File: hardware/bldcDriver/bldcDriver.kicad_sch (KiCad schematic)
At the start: 101 parts, among them J1 Conn_01x02, J2 Conn_01x06, J3 Conn_01x06, J4 Conn_01x03, J5 Conn_01x06, Q13 PMOS, Q14 S8050, U10 AMS1117, U2 STM32G431RBTx, U3 TPS5430DDA, U5 MPU6500, U6 TLV9062xD, U7 MT3608, U8 TLV9062xD, U9 TLV9062xD, Y1 25MHz

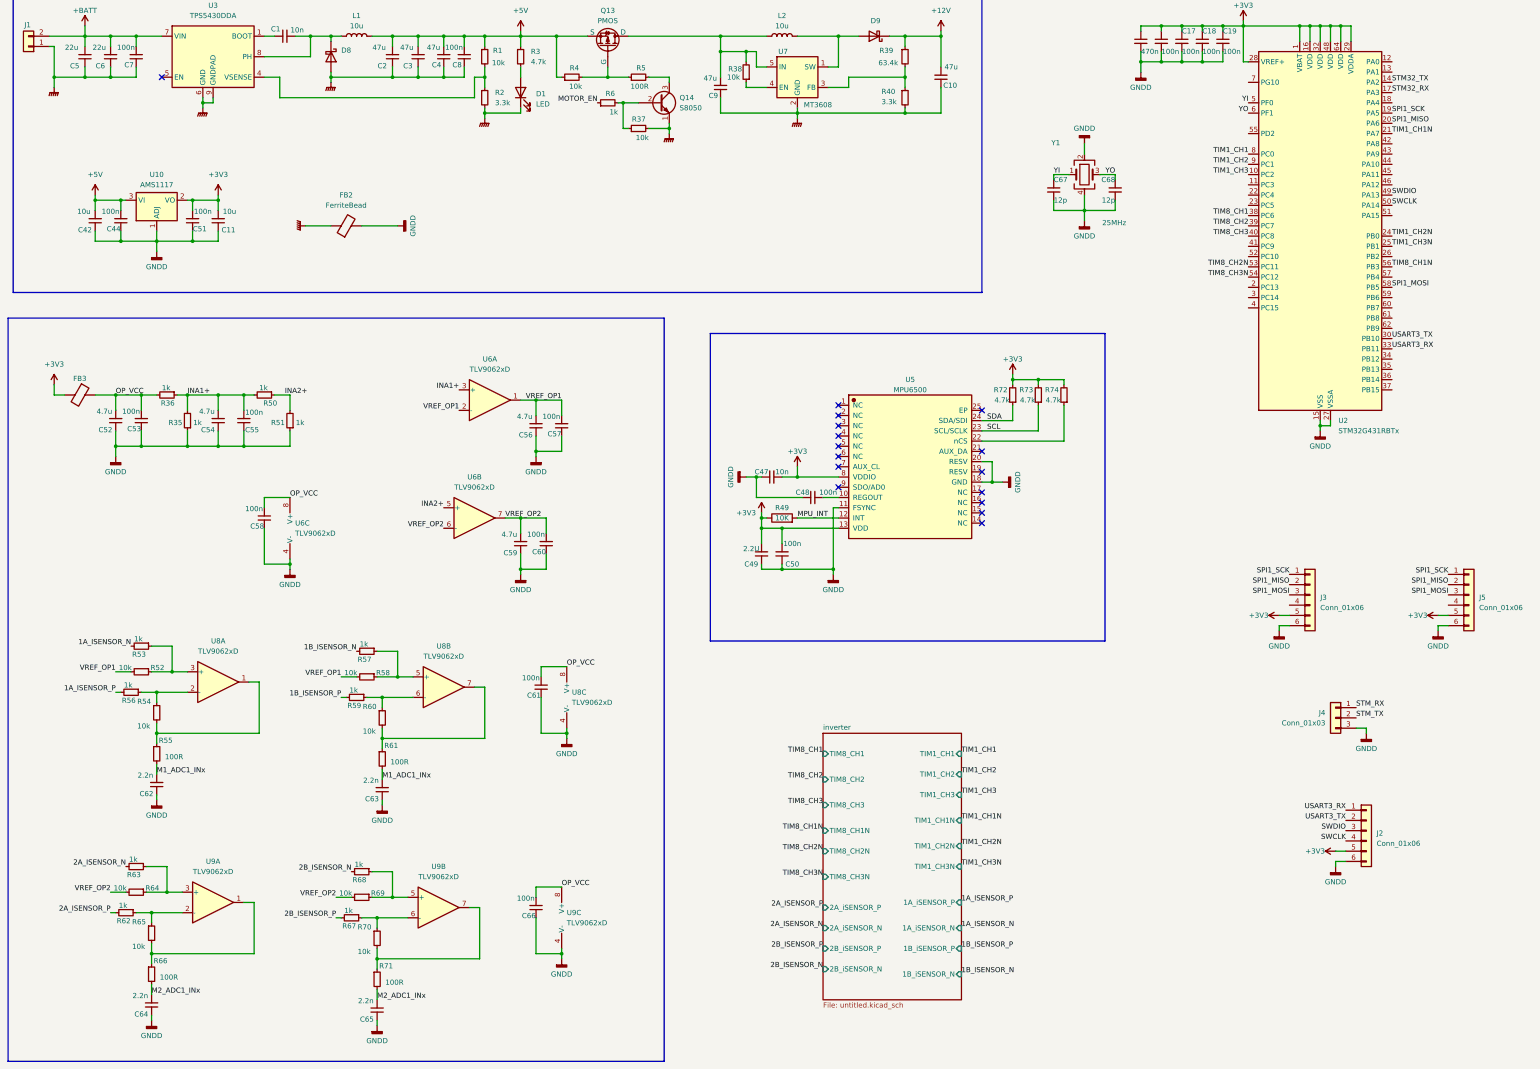
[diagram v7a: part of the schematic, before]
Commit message: update motorDriver pcb
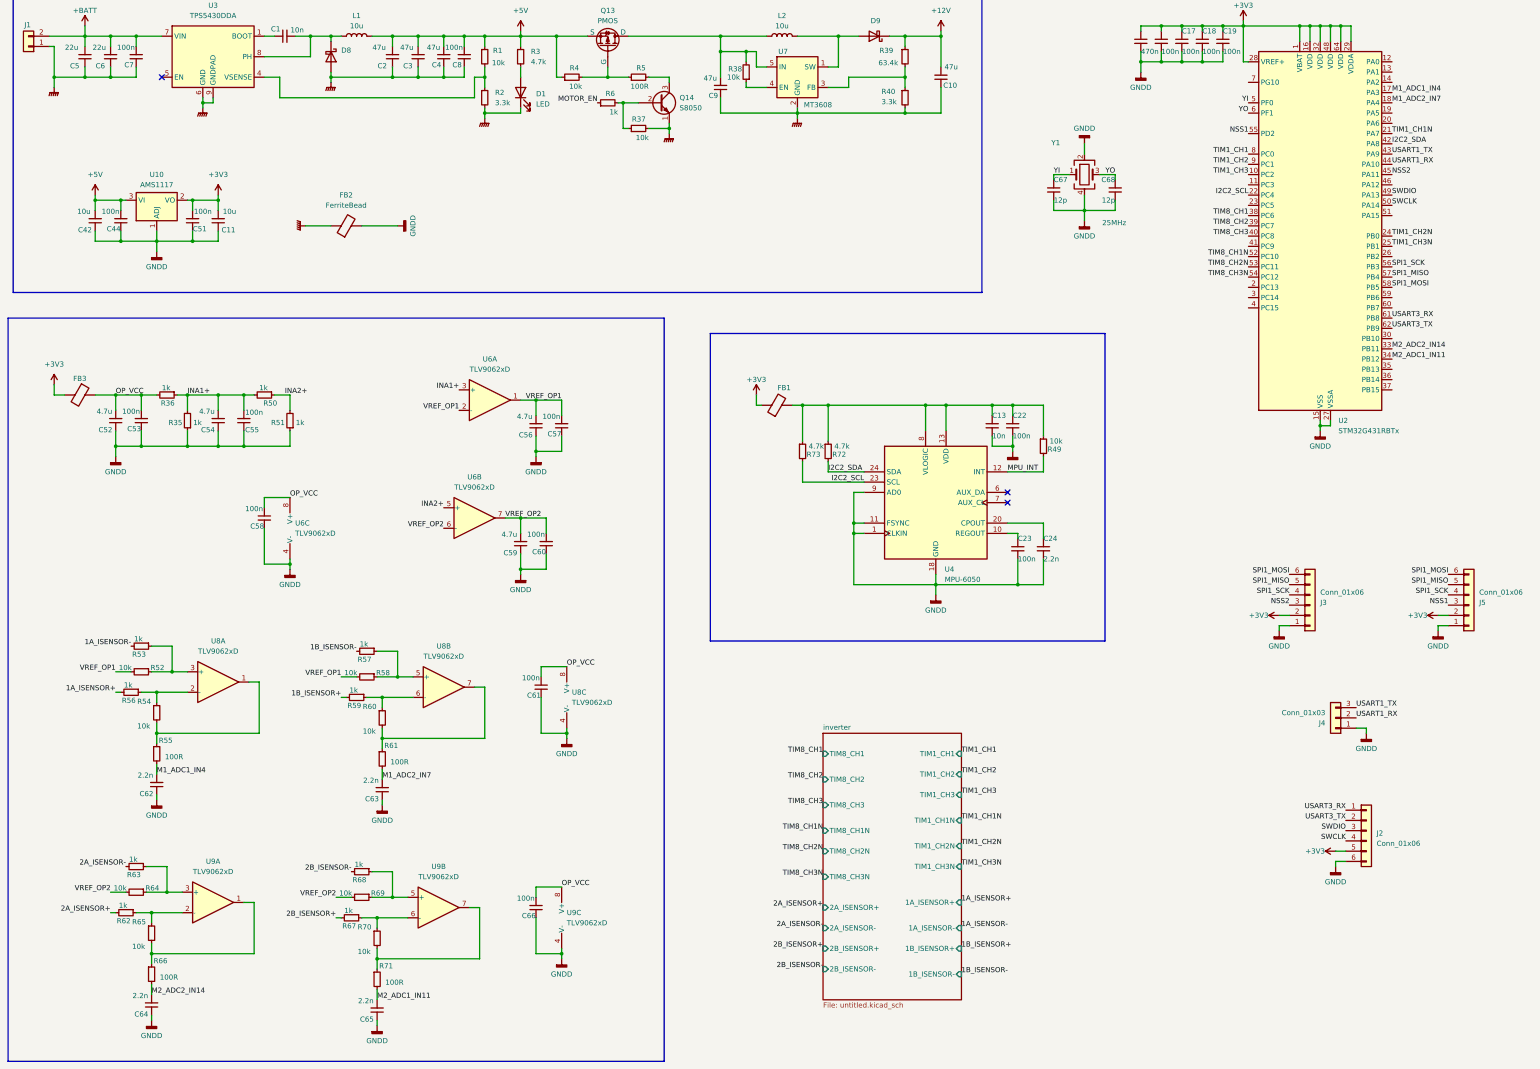
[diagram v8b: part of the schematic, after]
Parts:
- removed C47: 10n, Capacitor_SMD:C_0603_1608Metric_Pad1.08x0.95mm_HandSolder, symbol Device:C_Small
- removed C48, C50: 100n, Capacitor_SMD:C_0603_1608Metric_Pad1.08x0.95mm_HandSolder, symbol Device:C_Small
- removed C49: 2.2U, Capacitor_SMD:C_0603_1608Metric_Pad1.08x0.95mm_HandSolder, symbol Device:C_Small
- removed R49: 10K, Resistor_SMD:R_0603_1608Metric_Pad0.98x0.95mm_HandSolder, symbol Device:R
- removed R74: 4.7k, Resistor_SMD:R_0603_1608Metric_Pad0.98x0.95mm_HandSolder, symbol Device:R_Small
- removed U5: MPU6500, balancerDriver:QFN-24_L3.0-W3.0-P0.40-BL-EP, symbol bldcDriver:MPU6500
- added C13: 10n, Capacitor_SMD:C_0603_1608Metric_Pad1.08x0.95mm_HandSolder, symbol Device:C_Small
- added C22, C23: 100n, Capacitor_SMD:C_0603_1608Metric_Pad1.08x0.95mm_HandSolder, symbol Device:C_Small
- added C24: 2.2n, Capacitor_SMD:C_0603_1608Metric_Pad1.08x0.95mm_HandSolder, symbol Device:C_Small
- added FB1: FerriteBead, Capacitor_SMD:C_0603_1608Metric_Pad1.08x0.95mm_HandSolder, symbol Device:FerriteBead
- added R49: 10k, Resistor_SMD:R_0603_1608Metric_Pad0.98x0.95mm_HandSolder, symbol Device:R_Small
- added U4: MPU-6050, Sensor_Motion:InvenSense_QFN-24_4x4mm_P0.5mm, symbol Sensor_Motion:MPU-6050
- J2: footprint Connector_PinSocket_2.54mm:PinSocket_1x06_P2.54mm_Vertical -> Connector_PinHeader_2.54mm:PinHeader_1x06_P2.54mm_Vertical
- J3, J5: footprint balancerDriver:CONN-SMD_BM06B-GHS-TBT-LF-SN -> balancerDriver:CONN-SMD_6P-P1.00_MEGASTAR_ZX-SH1.0-6PWT
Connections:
- net SDA is gone; now on an unnamed net: R72.1
- net STM32_RX is gone; now on net M1_ADC1_IN4: U2.17 (PA3)
- net STM_RX is gone; now on net GNDD: J4.1 (Pin_1)
- net STM_TX is gone; now on net USART1_RX: J4.2 (Pin_2)
- net +3V3: now also J3.2 (Pin_2), J5.2 (Pin_2), FB1.1; no longer J3.5 (Pin_5), J5.5 (Pin_5), R72.2, R73.2
- net GNDD: now also J3.1 (Pin_1), J5.1 (Pin_1), C13.2, C22.2, C23.2, C24.2, U4.1 (CLKIN), U4.11 (FSYNC), U4.18 (GND), U4.9 (AD0); no longer J3.6 (Pin_6), J4.3 (Pin_3), J5.6 (Pin_6)
- net MPU_INT: now also R49.2, U4.12 (INT)
- net SPI1_MISO: now also J3.5 (Pin_5), J5.5 (Pin_5), U2.57 (PB4); no longer J3.2 (Pin_2), J5.2 (Pin_2), U2.20 (PA6)
- net SPI1_MOSI: now also J3.6 (Pin_6), J5.6 (Pin_6); no longer J3.3 (Pin_3), J5.3 (Pin_3)
- net SPI1_SCK: now also J3.4 (Pin_4), J5.4 (Pin_4), U2.56 (PB3); no longer J3.1 (Pin_1), J5.1 (Pin_1), U2.19 (PA5)
- net TIM8_CH1N: now also U2.52 (PC10); no longer U2.56 (PB3)
- net USART3_RX: now also U2.61 (PB8); no longer U2.33 (PB11)
- net USART3_TX: now also U2.62 (PB9); no longer U2.30 (PB10)
- net M1_ADC2_IN7: now reaches U2.18 (PA4)
- net M1_ADC2_IN7: now also C63.2, R61.2
- net I2C2_SCL: now reaches U2.22 (PC4)
- net I2C2_SCL: now also R73.2, U4.23 (SCL)
- net M2_ADC1_IN11: now reaches U2.34 (PB12)
- net M2_ADC1_IN11: now also C65.2, R71.2
- net I2C2_SDA: now reaches U2.42 (PA8)
- net I2C2_SDA: now also R72.2, U4.24 (SDA)
- net USART1_TX: now reaches U2.43 (PA9)
- net USART1_TX: now also J4.3 (Pin_3)
- net USART1_RX: now reaches U2.44 (PA10)
- net NSS2: now reaches U2.45 (PA11)
- net NSS2: now also J3.3 (Pin_3)
- net NSS1: now reaches U2.55 (PD2)
- net NSS1: now also J5.3 (Pin_3)
- net 1A_ISENSOR_N renamed 1A_ISENSOR-
- net 1A_ISENSOR_P renamed 1A_ISENSOR+
- net 1B_ISENSOR_N renamed 1B_ISENSOR-
- net 1B_ISENSOR_P renamed 1B_ISENSOR+
- net 2A_ISENSOR_N renamed 2A_ISENSOR-
- net 2A_ISENSOR_P renamed 2A_ISENSOR+
- net 2B_ISENSOR_N renamed 2B_ISENSOR-
- net 2B_ISENSOR_P renamed 2B_ISENSOR+
- net M1_ADC1_INx renamed M1_ADC1_IN4
- net M1_ADC1_IN4: no longer C63.2, R61.2
- net M2_ADC1_INx renamed M2_ADC2_IN14
- net M2_ADC2_IN14: now also U2.33 (PB11); no longer C65.2, R71.2
- net SCL: no longer names the net of R73.1
- net SCL: now also C13.1, C22.1, FB1.2, R49.1, U4.13 (VDD), U4.8 (VLOGIC)
- net STM32_TX: no longer names the net of U2.14 (PA2)
- new net: C23.1, U4.10 (REGOUT)
- new net: C24.1, U4.20 (CPOUT)
- no-connect marks 16 -> 3
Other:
- sheet inverter ports: added 1A_ISENSOR+, 1A_ISENSOR-, 1B_ISENSOR+, 1B_ISENSOR-, 2A_ISENSOR+, 2A_ISENSOR-, 2B_ISENSOR+, 2B_ISENSOR-; removed 1A_iSENSOR_N, 1A_iSENSOR_P, 1B_iSENSOR_N, 1B_iSENSOR_P, 2A_iSENSOR_N, 2A_iSENSOR_P, 2B_iSENSOR_N, 2B_iSENSOR_P
- moved on the sheet: J4
